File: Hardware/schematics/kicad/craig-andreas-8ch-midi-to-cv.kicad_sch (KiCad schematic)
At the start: 56 parts, among them J1 MIDI IN, J8 Power Input, U1 Teensy4.1, U10 DAC8568, U11 L7805, U2 DAC8568, U3 ADG5206BRUZ, U4 74HC14, U5 TL074HID, U6 REF102AU, U7 DAC8568, U8 DAC8568, U9 DAC8568

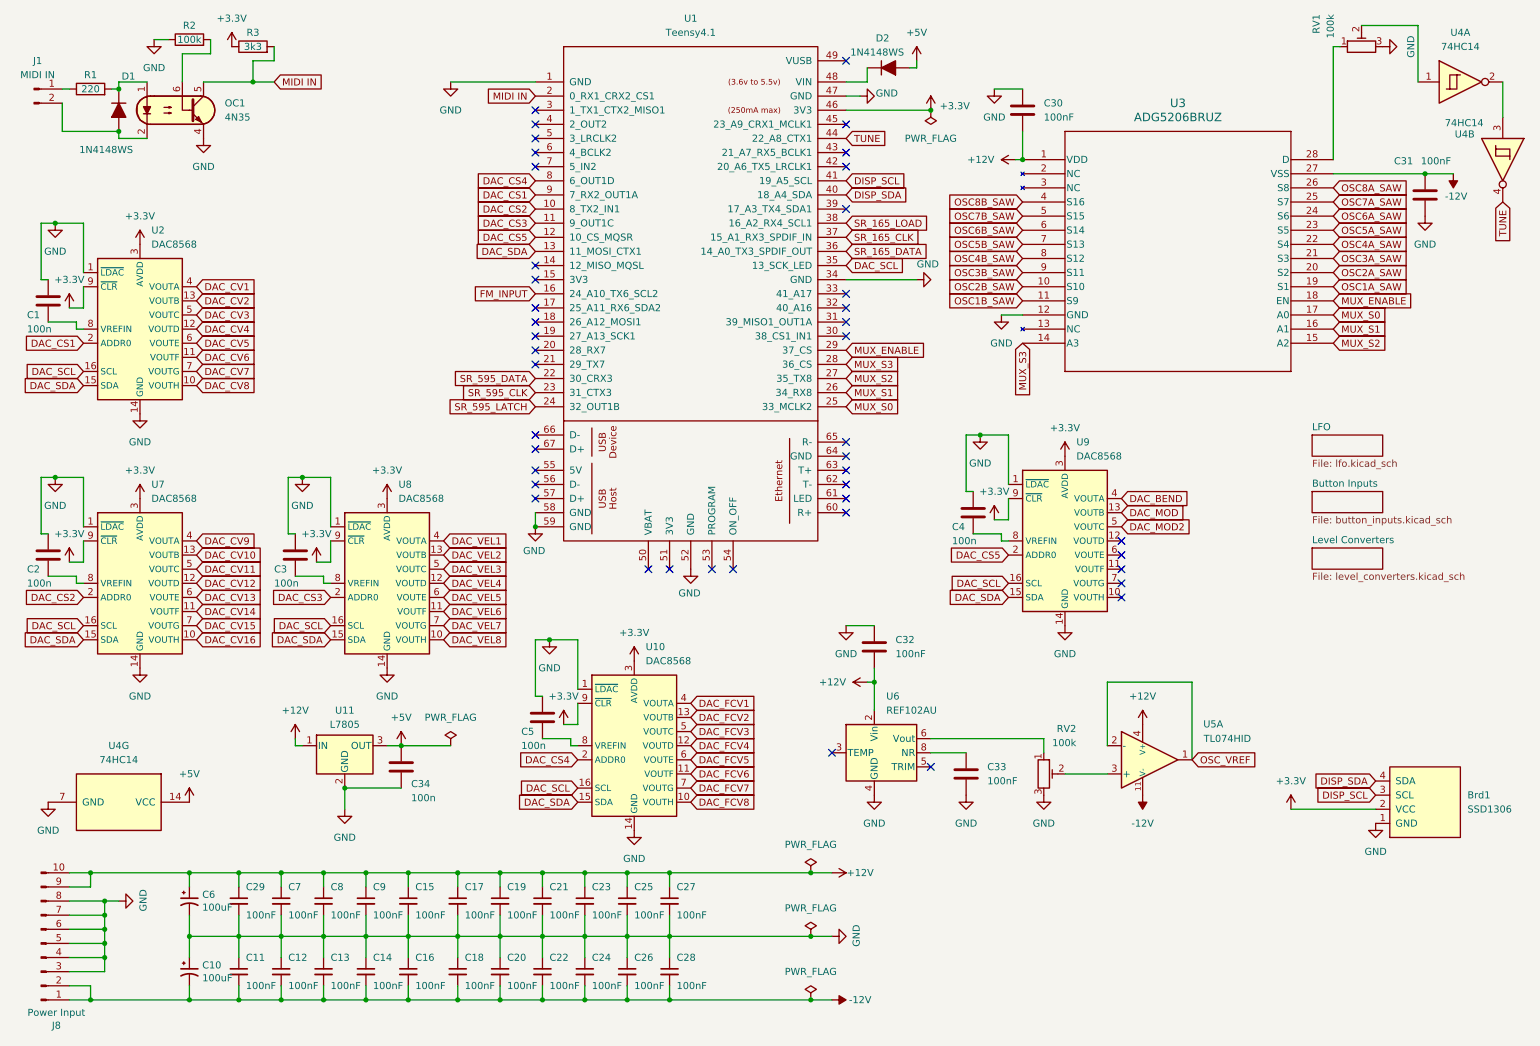
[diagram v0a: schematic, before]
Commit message: Modify schematics to suit a complete Eurorack PCB design
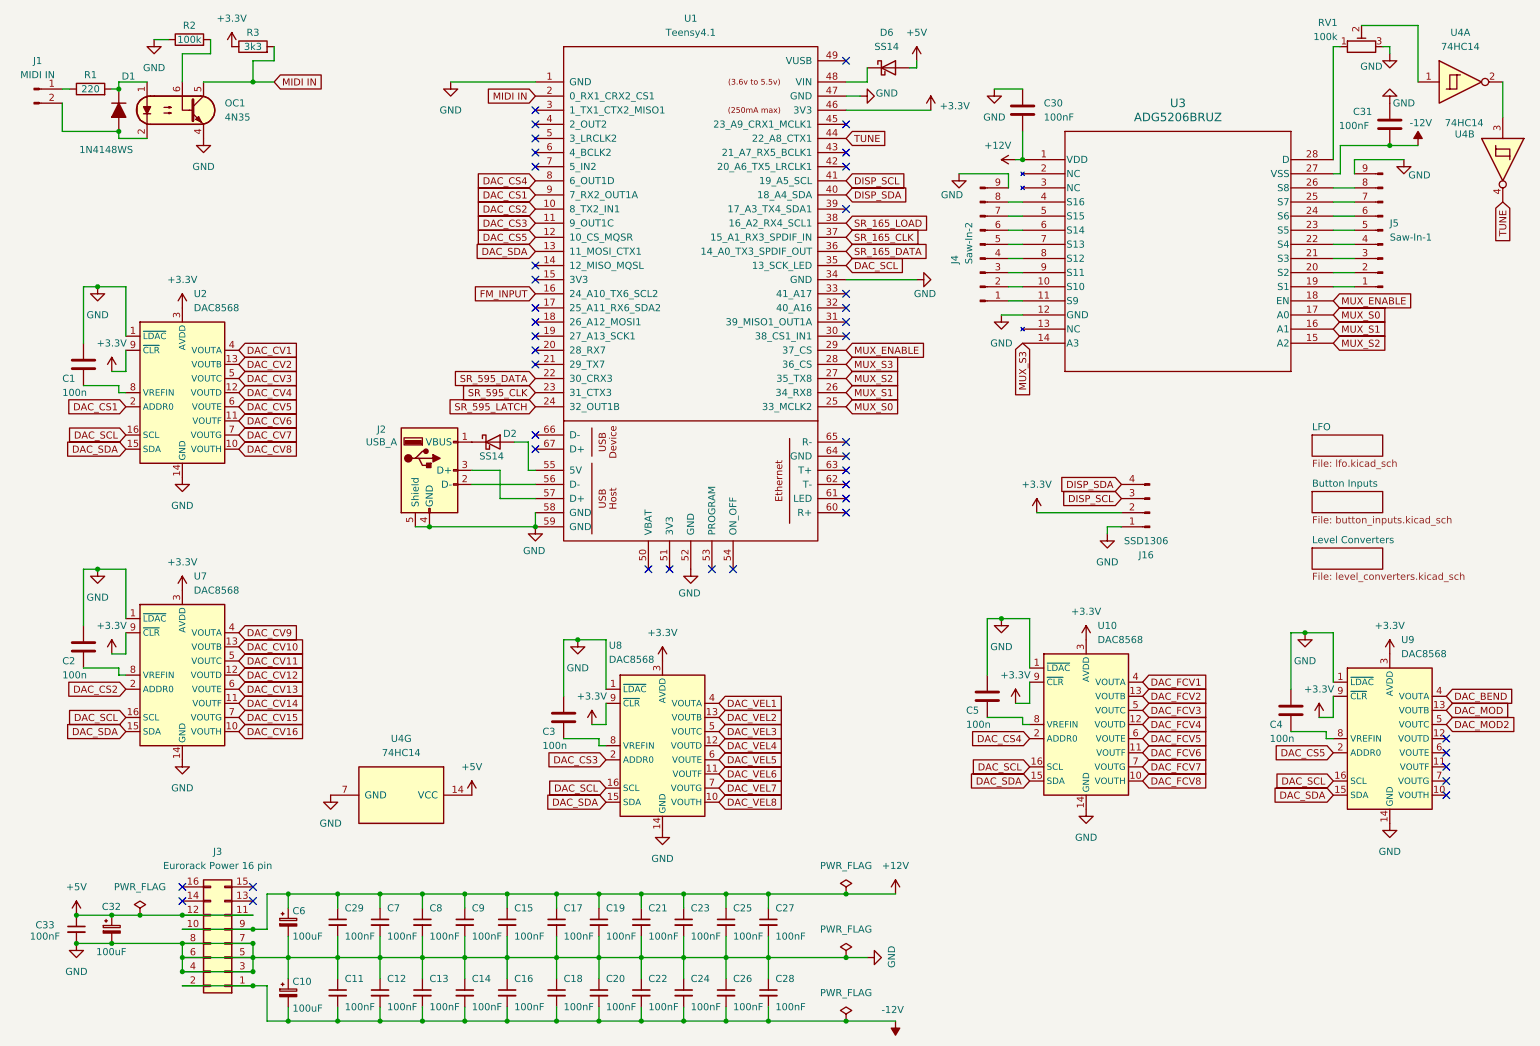
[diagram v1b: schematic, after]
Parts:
- removed Brd1: SSD1306, SSD1306:128x64OLED, symbol SSD1306-128x64_OLED:SSD1306
- removed C32, C33: 100nF, Capacitor_SMD:C_0805_2012Metric_Pad1.18x1.45mm_HandSolder, symbol Device:C
- removed C34: 100n, Capacitor_SMD:C_0805_2012Metric_Pad1.18x1.45mm_HandSolder, symbol Device:C
- removed D2: 1N4148WS, Diode_SMD:D_SOD-323_HandSoldering, symbol PCM_Diode_AKL:1N4148WS
- removed J8: Power Input, Connector_IDC:IDC-Header_2x05_P2.54mm_Vertical, symbol Connector:Conn_01x10_Male
- removed RV2: 100k, PCM_Potentiometer_THT_AKL:Potentiometer_Runtron_RM-065_Vertical, symbol Device:R_Potentiometer_Trim
- removed U11: L7805, PCM_4ms_Package_TO:TO-220-3_Vertical, symbol Regulator_Linear:L7805
- removed U5: TL074HID, PCM_Package_SO_AKL:SOIC-14_3.9x8.7mm_P1.27mm, symbol PCM_Amplifier_Operational_AKL:TL074HID
- removed U6: REF102AU, Package_SO:SOIC-8_3.9x4.9mm_P1.27mm, symbol Reference_Voltage:REF102AU
- added C32: 100uF, Capacitor_THT:CP_Radial_D8.0mm_P3.50mm, symbol Device:C_Polarized_Small
- added C33: 100nF, Capacitor_SMD:C_0805_2012Metric_Pad1.18x1.45mm_HandSolder, symbol Device:C_Small
- added D2, D6: SS14, Diode_SMD:D_SMA_Handsoldering, symbol Diode:SS14
- added J16: SSD1306, Connector_JST:JST_XH_B4B-XH-A_1x04_P2.50mm_Vertical, symbol Connector:Conn_01x04_Pin
- added J2: USB_A, Connector_JST:JST_XH_B3B-XH-A_1x03_P2.50mm_Vertical, symbol Connector:USB_A
- added J3: Eurorack Power 16 pin, Connector_IDC:IDC-Header_2x08_P2.54mm_Vertical, symbol Connector_Generic:Conn_02x08_Odd_Even
- added J4: Saw-In-2, Connector_JST:JST_XH_B9B-XH-A_1x09_P2.50mm_Vertical, symbol Connector:Conn_01x09_Pin
- added J5: Saw-In-1, Connector_JST:JST_XH_B9B-XH-A_1x09_P2.50mm_Vertical, symbol Connector:Conn_01x09_Pin
- C10, C6: footprint Capacitor_THT:CP_Radial_D5.0mm_P2.00mm -> Capacitor_THT:CP_Radial_D8.0mm_P3.50mm; symbol Device:CP1_Small -> Device:C_Polarized_Small
- J1: footprint Eurocad:MIDI_DIN5 -> Connector_JST:JST_XH_B2B-XH-A_1x02_P2.50mm_Vertical
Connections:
- net +12V: now also J3.10 (Pin_10), J3.9 (Pin_9)
- net +3.3V: now also J16.2 (Pin_2)
- net +5V: now also C32.1, C33.1, D6.2 (A), J3.11 (Pin_11), J3.12 (Pin_12)
- net -12V: now also J3.1 (Pin_1), J3.2 (Pin_2)
- net DISP_SCL: now also J16.3 (Pin_3)
- net DISP_SDA: now also J16.4 (Pin_4)
- net GND: now also C32.2, C33.2, J16.1 (Pin_1), J2.4 (GND), J2.5 (Shield), J3.3 (Pin_3), J3.4 (Pin_4), J3.5 (Pin_5), J3.6 (Pin_6), J3.7 (Pin_7), J3.8 (Pin_8), J4.9 (Pin_9), J5.9 (Pin_9)
- net at U1.48 (VIN): now also D6.1 (K)
- net at U1.55 (5V): now also D2.2 (A)
- net at U1.56 (D-): now also J2.2 (D-)
- net at U1.57 (D+): now also J2.3 (D+)
- net OSC1A_SAW: no longer names the net of U3.19 (S1)
- net OSC1A_SAW: now also J5.1 (Pin_1)
- net OSC1B_SAW: no longer names the net of U3.11 (S9)
- net OSC1B_SAW: now also J4.1 (Pin_1)
- net OSC2A_SAW: no longer names the net of U3.20 (S2)
- net OSC2A_SAW: now also J5.2 (Pin_2)
- net OSC2B_SAW: no longer names the net of U3.10 (S10)
- net OSC2B_SAW: now also J4.2 (Pin_2)
- net OSC3A_SAW: no longer names the net of U3.21 (S3)
- net OSC3A_SAW: now also J5.3 (Pin_3)
- net OSC3B_SAW: no longer names the net of U3.9 (S11)
- net OSC3B_SAW: now also J4.3 (Pin_3)
- net OSC4A_SAW: no longer names the net of U3.22 (S4)
- net OSC4A_SAW: now also J5.4 (Pin_4)
- net OSC4B_SAW: no longer names the net of U3.8 (S12)
- net OSC4B_SAW: now also J4.4 (Pin_4)
- net OSC5A_SAW: no longer names the net of U3.23 (S5)
- net OSC5A_SAW: now also J5.5 (Pin_5)
- net OSC5B_SAW: no longer names the net of U3.7 (S13)
- net OSC5B_SAW: now also J4.5 (Pin_5)
- net OSC6A_SAW: no longer names the net of U3.24 (S6)
- net OSC6A_SAW: now also J5.6 (Pin_6)
- net OSC6B_SAW: no longer names the net of U3.6 (S14)
- net OSC6B_SAW: now also J4.6 (Pin_6)
- net OSC7A_SAW: no longer names the net of U3.25 (S7)
- net OSC7A_SAW: now also J5.7 (Pin_7)
- net OSC7B_SAW: no longer names the net of U3.5 (S15)
- net OSC7B_SAW: now also J4.7 (Pin_7)
- net OSC8A_SAW: no longer names the net of U3.26 (S8)
- net OSC8A_SAW: now also J5.8 (Pin_8)
- net OSC8B_SAW: no longer names the net of U3.4 (S16)
- net OSC8B_SAW: now also J4.8 (Pin_8)
- new net: D2.1 (K), J2.1 (VBUS)
- no-connect marks 43 -> 42
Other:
- moved on the sheet: C1, C11, C12, C13, C14, C15, C16, C17, C18, C19, C2, C20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

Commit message: Remove LFO in favor of standalone LFO and create PCB. FM Input still exists in case it's needed.
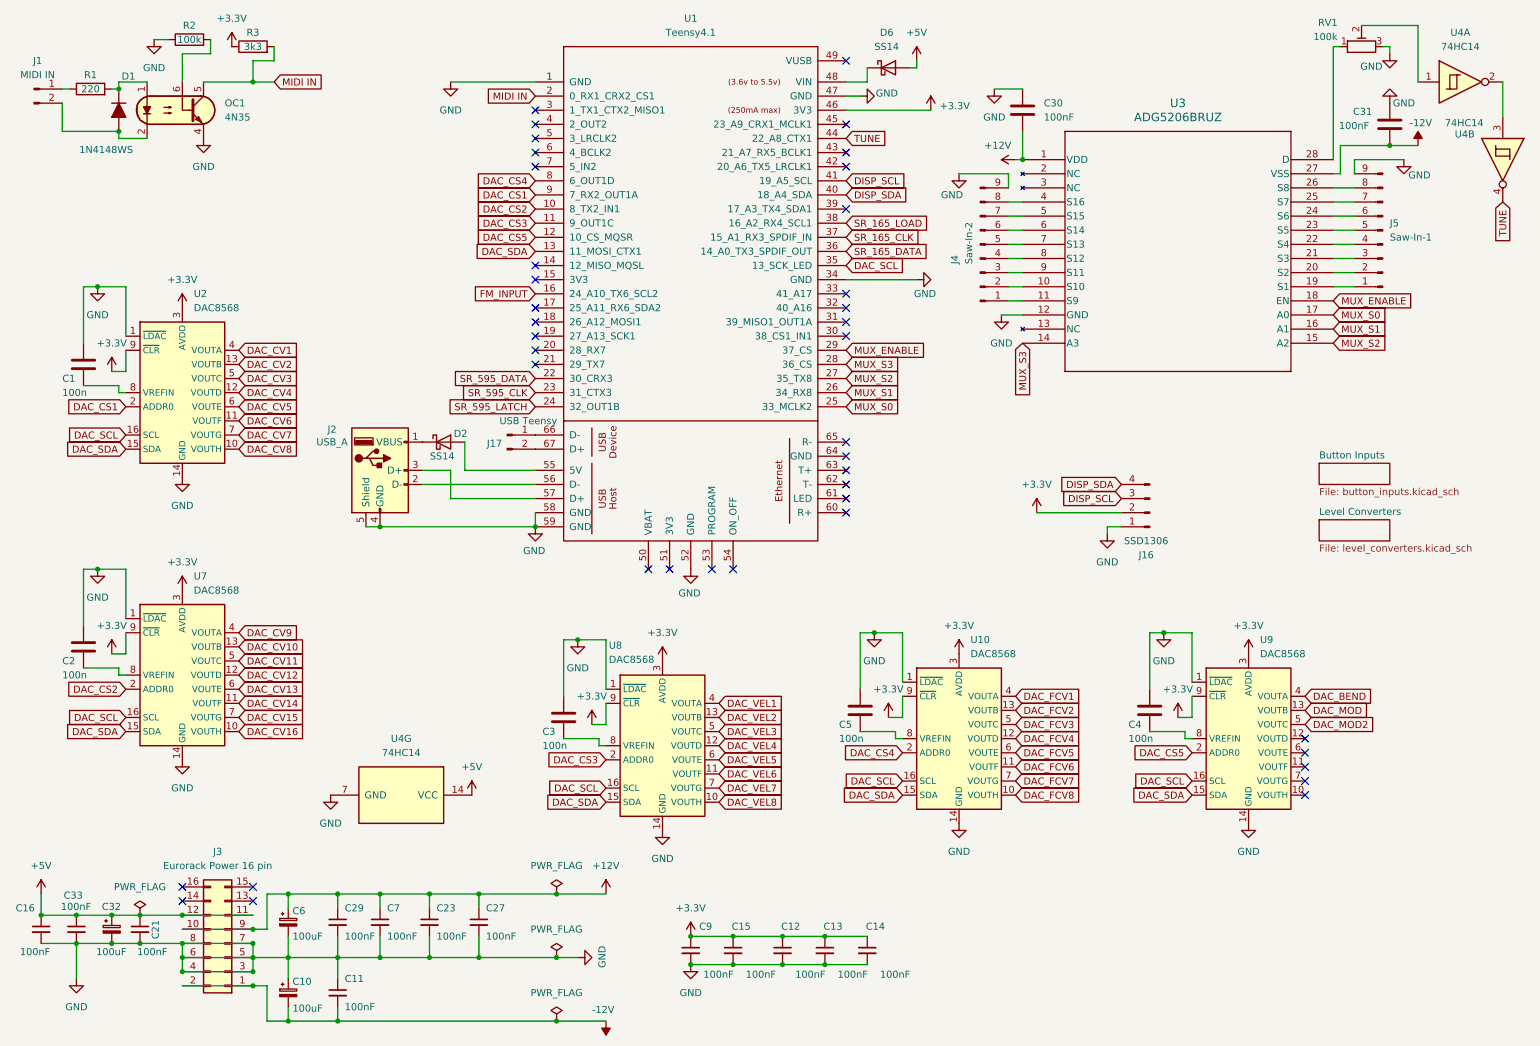
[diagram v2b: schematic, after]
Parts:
- removed C17, C18, C19, C20, C22, C24, C25, C26, C28, C8: 100nF, Capacitor_SMD:C_0805_2012Metric_Pad1.18x1.45mm_HandSolder, symbol Device:C_Small
- added J17: USB Teensy, Connector_JST:JST_XH_B2B-XH-A_1x02_P2.50mm_Vertical, symbol Connector:Conn_01x02_Pin
- RV1: footprint PCM_Potentiometer_THT_AKL:Potentiometer_Runtron_RM-065_Vertical -> Potentiometer_THT:Potentiometer_Runtron_RM-065_Vertical
- U4: footprint Package_DIP:DIP-14_W7.62mm_LongPads -> Package_SO:SOIC-14_3.9x8.7mm_P1.27mm
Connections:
- net +12V: no longer C15.1, C21.1, C9.1
- net +3.3V: now also C12.1, C13.1, C14.1, C15.1, C9.1
- net +5V: now also C16.1, C21.1
- net -12V: no longer C12.2, C13.2, C14.2, C16.2
- net GND: now also C12.2, C13.2, C14.2, C16.2; no longer C12.1, C13.1, C14.1, C16.1
- net at U1.66 (D-): now also J17.1 (Pin_1)
- net at U1.67 (D+): now also J17.2 (Pin_2)
- no-connect marks 42 -> 40
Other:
- removed sheet LFO
- moved on the sheet: C12, C13, C14, C15, C16, C21, C23, C27, C4, C5, C9, D2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
